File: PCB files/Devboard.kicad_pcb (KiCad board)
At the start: 2 copper layers, 44.9 x 54.7 mm, 41 parts, among them IC1 MPU-6500, J1 USB_C_Receptacle_USB2.0_14P, J2 Conn_01x03, J3 Conn_01x20, J4 Conn_01x20, J5 JST_2mm_LiPo, SW1 SW_Push, U1 RP2040, U2 NCP1117-3.3_SOT223, U3 W25Q128JVS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

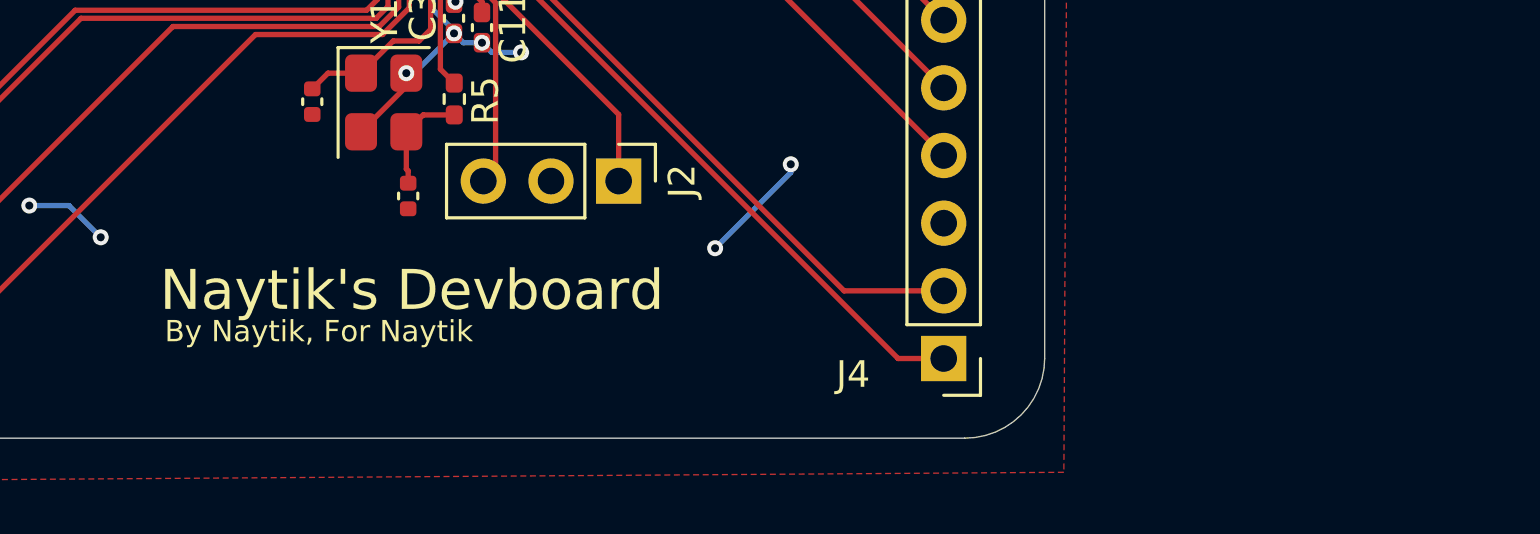
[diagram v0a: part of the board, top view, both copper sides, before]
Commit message: I added a tic tac toe board to the back
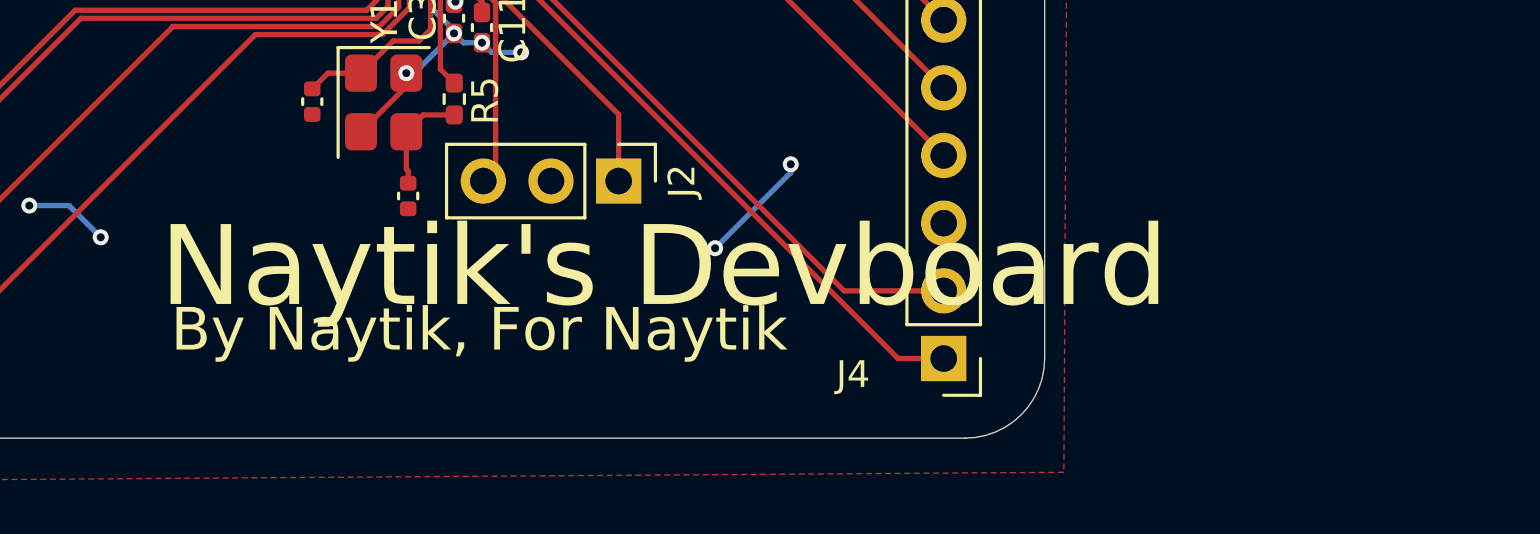
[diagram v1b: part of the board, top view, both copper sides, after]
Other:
- board text added: "Play Tic Tac Toe."

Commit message: added better art
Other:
- board text removed: "Play Tic Tac Toe."

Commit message: added better silkscreen art
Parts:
- added G***: LOGO, F16art:f16-40mm, B.Cu at (195.8, 88.9)
